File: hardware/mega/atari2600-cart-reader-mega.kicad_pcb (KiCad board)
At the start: 2 copper layers, 101.6 x 53.3 mm, 12 parts, among them J1 Atari 2600 Cartridge-Slot, Q1 BC327, SW1 Reset, SW2 Read

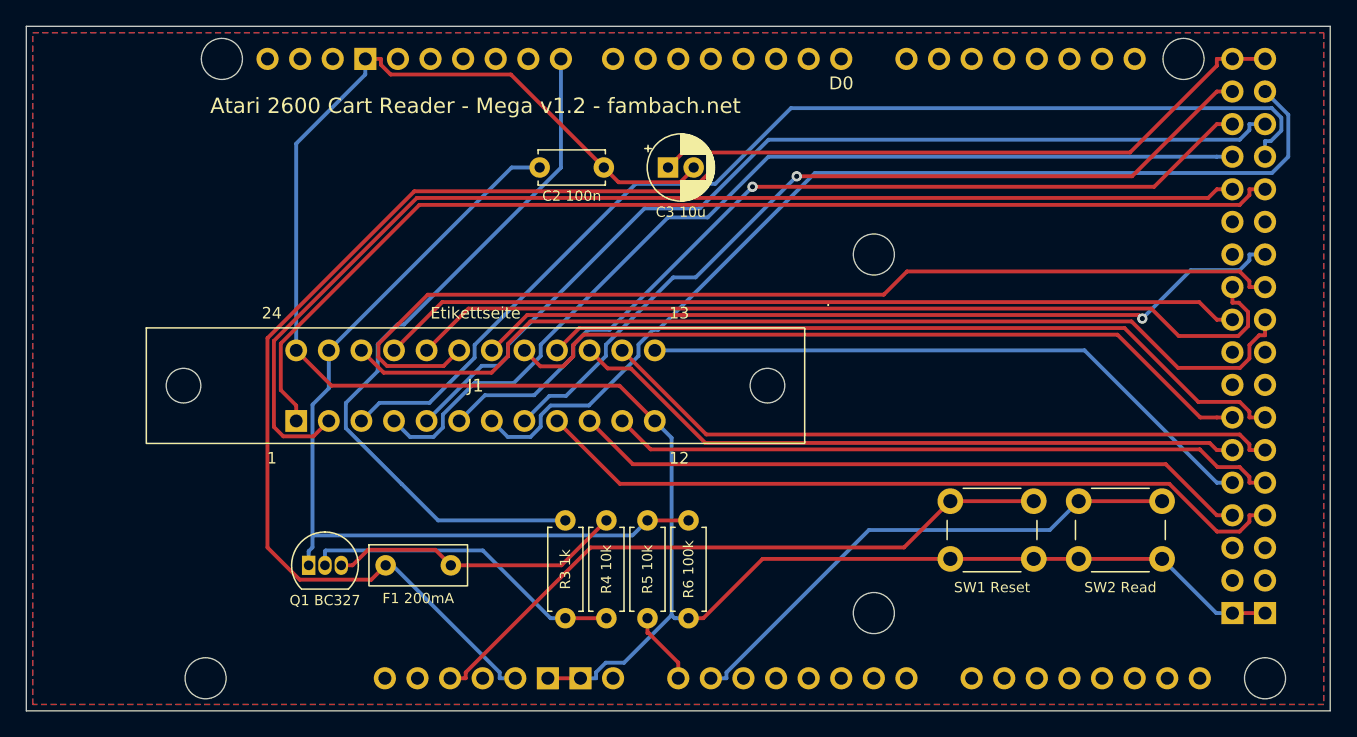
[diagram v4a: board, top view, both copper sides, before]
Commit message: Uno/Nano: address bus via two 74HC595 on SPI, MCP23017 boards kept as variants
hal.h selects the MCP23017 with #define ADDR_MCP23017.

Co-Authored-By: Claude Opus 5.5 <noreply@anthropic.com>
Claude-Session: https://claude.ai/code/session_015VQCpzuZ22TPQEmx9cLrbH
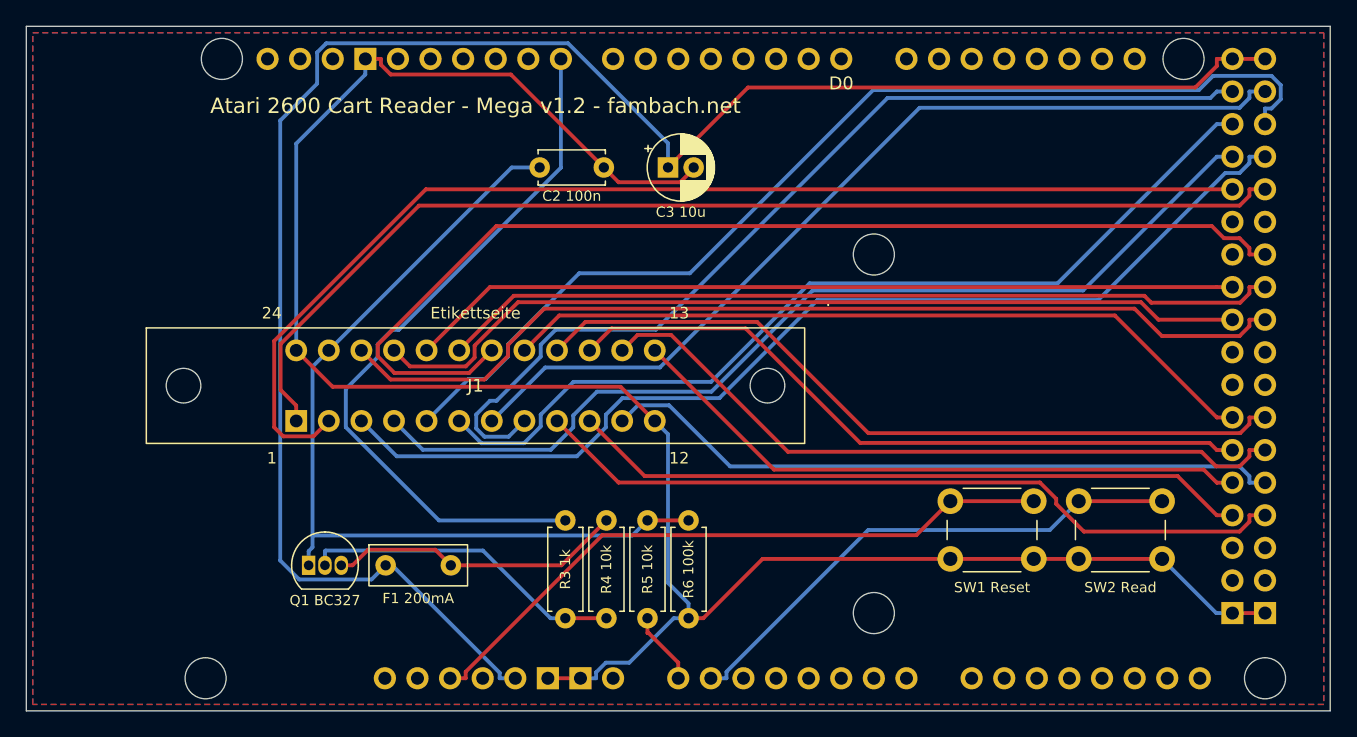
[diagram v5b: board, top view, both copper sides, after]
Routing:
- net /A12: track 63.8 -> 85.2 mm, vias 1 -> 0
- net /A10: track 80.3 -> 65.6 mm
- net +5V: track 132.7 -> 147.2 mm
- net /A0: track 66.3 -> 75.5 mm, vias 1 -> 0
- net /A1: track 78.5 -> 71.2 mm
- net /A3: track 75.7 -> 82.4 mm
- net /A11: track 70.4 -> 64.8 mm
- net /A5: track 86.5 -> 82.1 mm
- net /D4: track 53.6 -> 55.7 mm
- net /A8: track 77.7 -> 75.9 mm
- net /A9: track 67.5 -> 69.0 mm
- net /A2: track 70.3 -> 71.8 mm, vias 1 -> 0
- net /D6: track 59.0 -> 60.5 mm
- net /D5: track 53.3 -> 54.7 mm
- net /D2: track 52.3 -> 53.4 mm
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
